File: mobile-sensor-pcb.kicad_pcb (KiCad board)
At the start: 2 copper layers, 101.6 x 53.3 mm, 27 parts, among them U1 NCP551

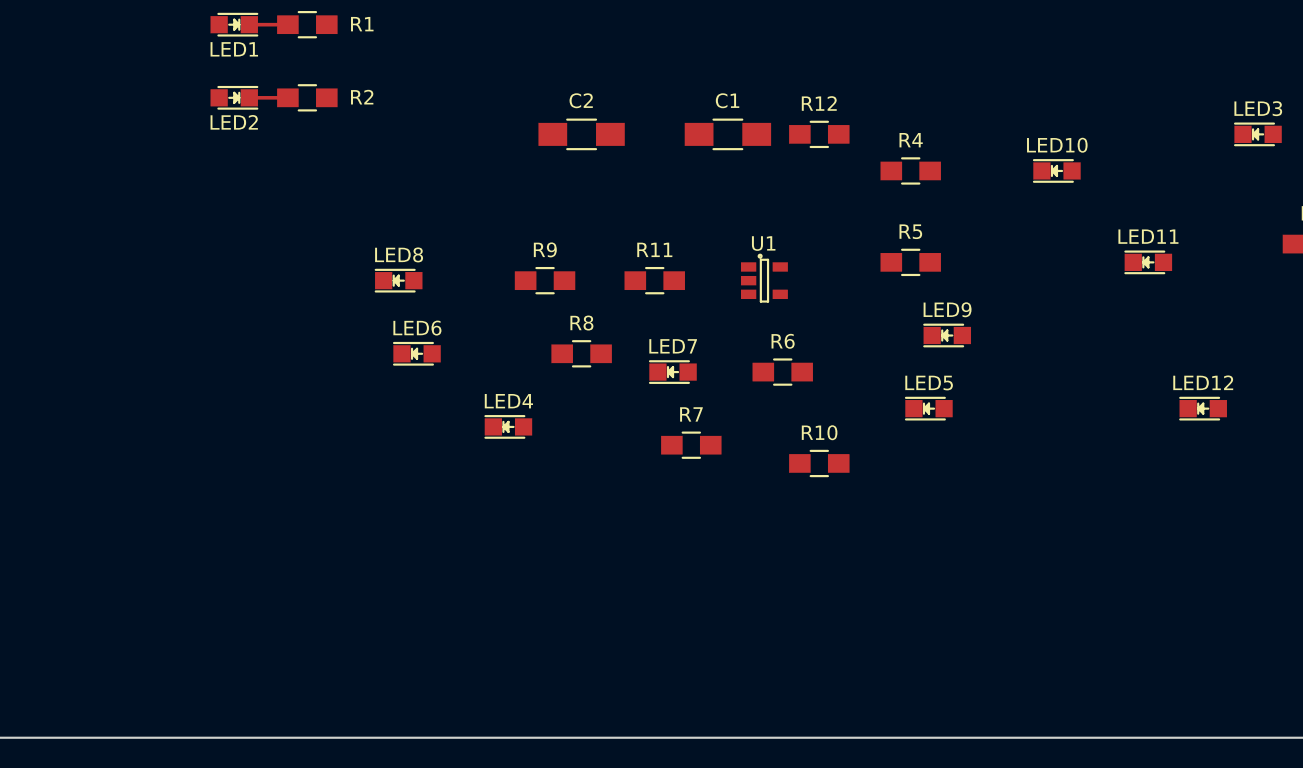
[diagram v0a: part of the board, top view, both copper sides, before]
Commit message: Add more components and footprints
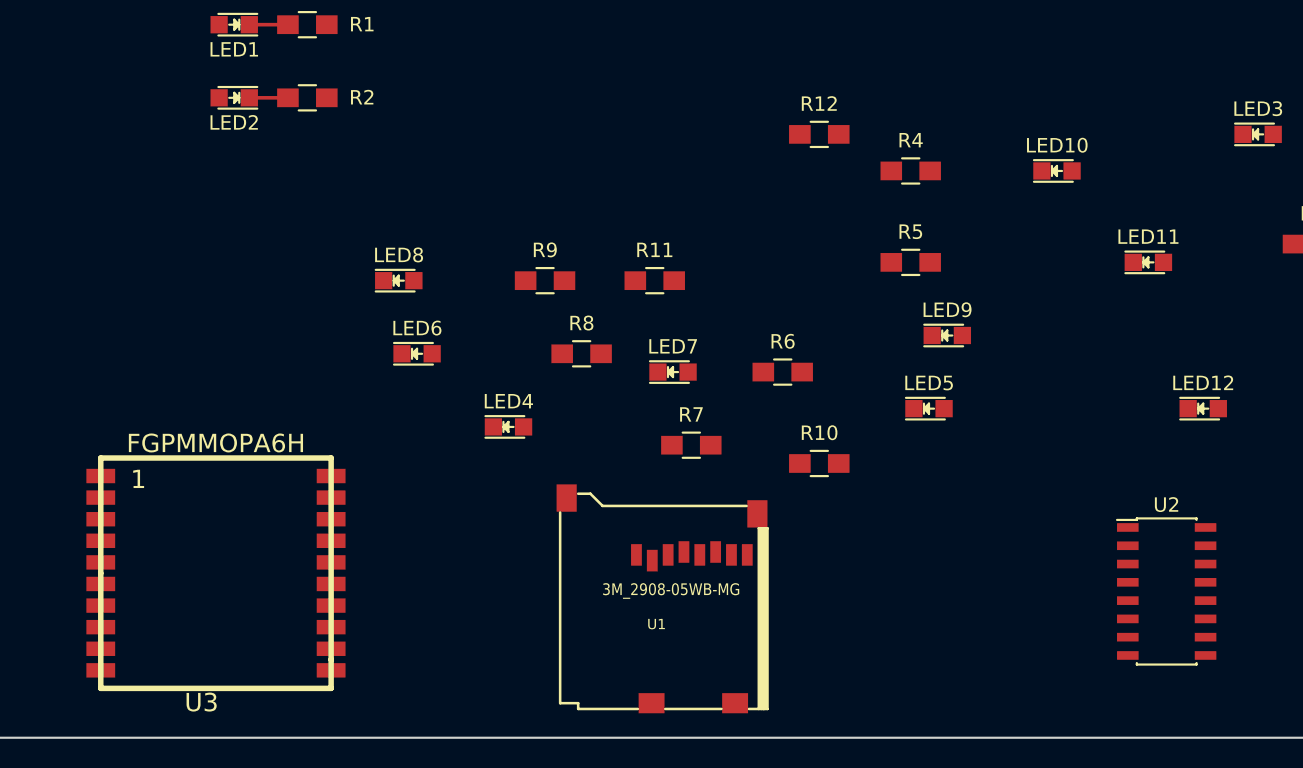
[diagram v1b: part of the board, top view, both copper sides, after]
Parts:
- removed C1: 10 uF, Capacitors_SMD:C_1206_HandSoldering
- removed C2: C_Small, Capacitors_SMD:C_1206_HandSoldering
- added U2: 74HC4050, Housings_SOIC:SOIC-16_3.9x9.9mm_Pitch1.27mm, F.Cu at (132.1, 142.2)
- added U3: FGPMMOPA6H, rascalmicro-kicad-footprints:FGPMMOPA6H, F.Cu at (66.0, 141.0)
- U1: value NCP551 -> 3M_2908-05WB-MG; footprint Housings_SOT-23_SOT-143_TSOT-6:SOT-23-5 -> rascalmicro-kicad-footprints:3M_2908-05WB-MG
- moved U1 21.0 mm to (95.2, 139.7)

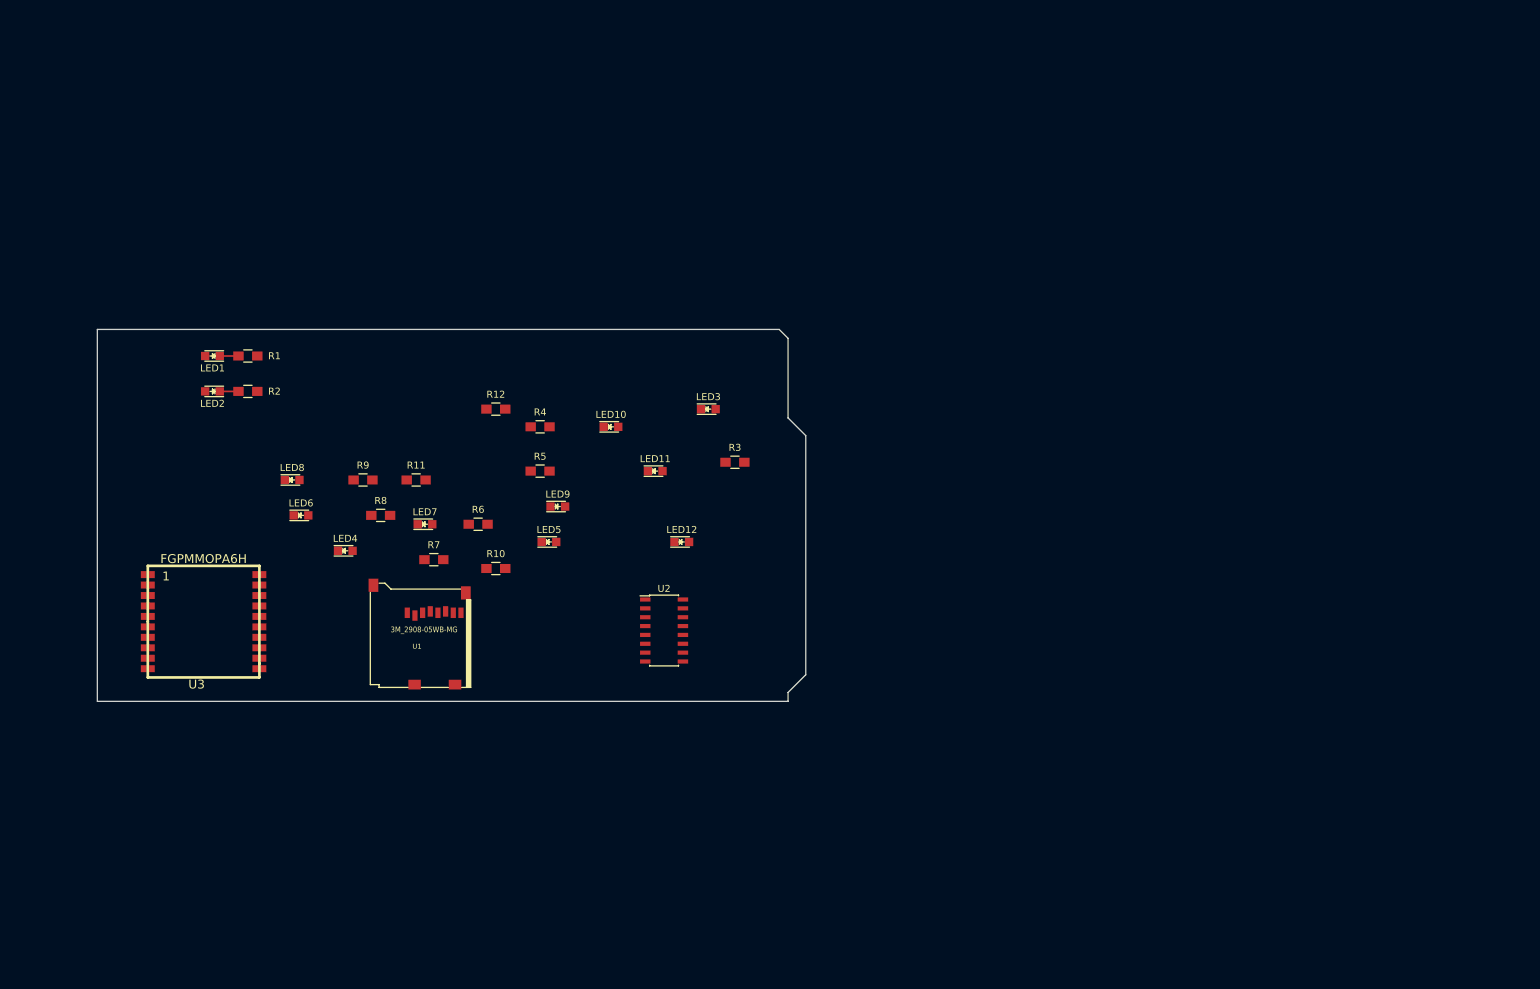
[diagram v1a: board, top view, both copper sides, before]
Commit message: More components, plus update footprint library rev
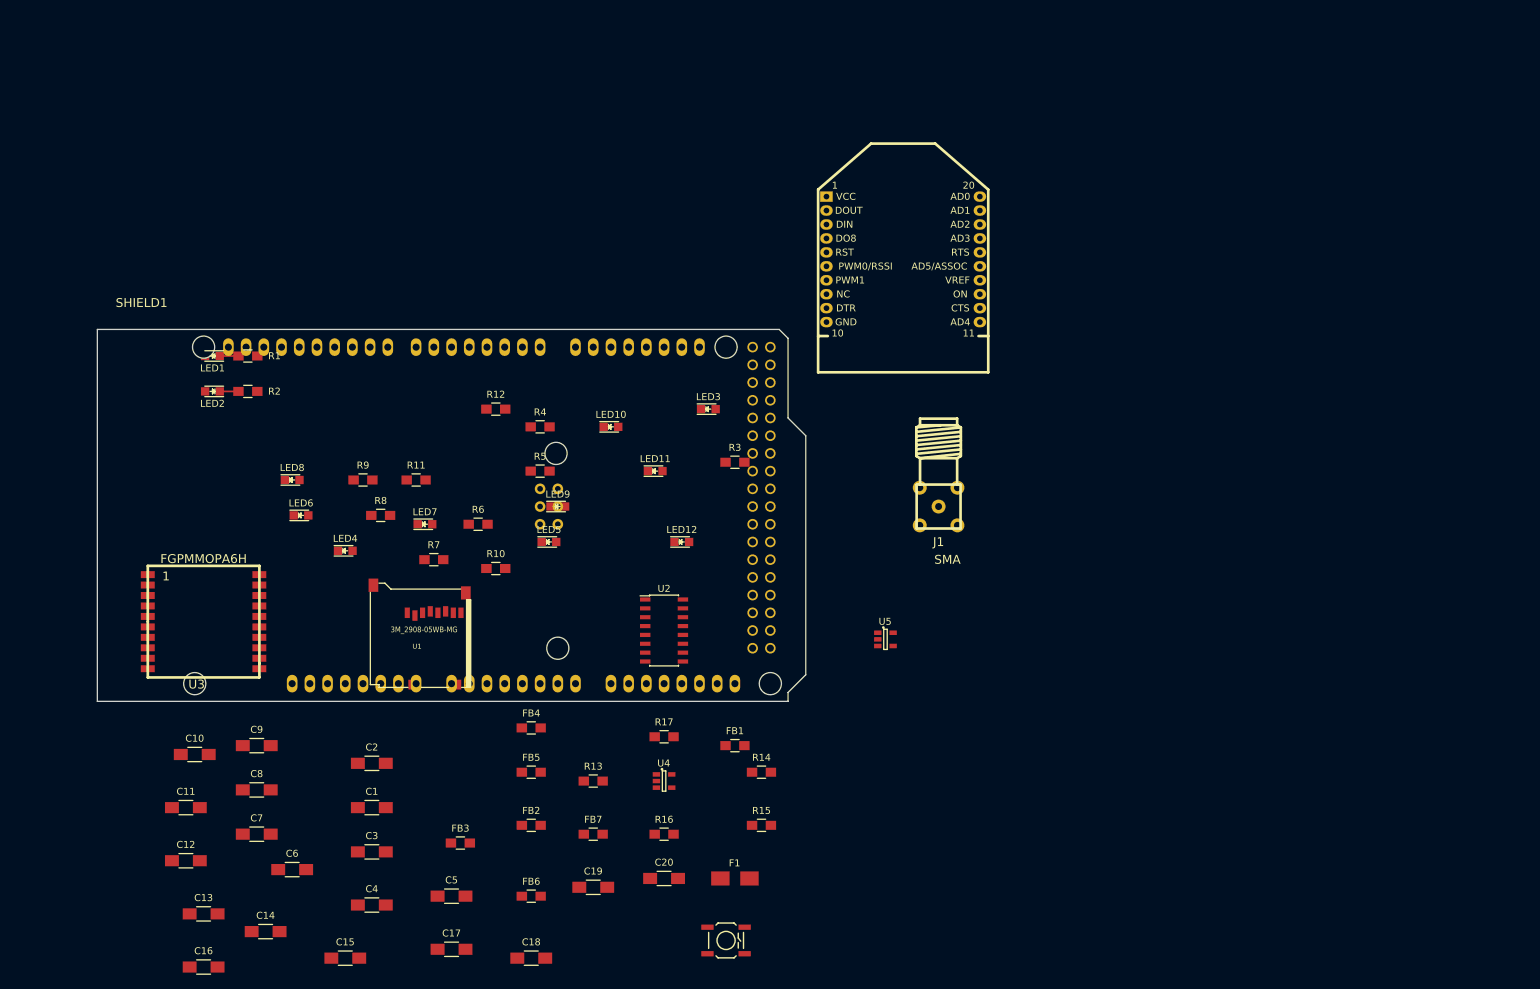
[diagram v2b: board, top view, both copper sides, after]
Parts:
- added C1: 10 uF, Capacitors_SMD:C_1206_HandSoldering, F.Cu at (90.2, 167.6)
- added C10: 10 uF, Capacitors_SMD:C_1206_HandSoldering, F.Cu at (64.8, 160.0)
- added C11: 10 uF, Capacitors_SMD:C_1206_HandSoldering, F.Cu at (63.5, 167.6)
- added C12: 10 uF, Capacitors_SMD:C_1206_HandSoldering, F.Cu at (63.5, 175.3)
- added C13: 2.2 uF, Capacitors_SMD:C_1206_HandSoldering, F.Cu at (66.0, 182.9)
- added C14: 100 nF, Capacitors_SMD:C_1206_HandSoldering, F.Cu at (74.9, 185.4)
- added C15: 100 nF, Capacitors_SMD:C_1206_HandSoldering, F.Cu at (86.4, 189.2)
- added C16: 100 nF, Capacitors_SMD:C_1206_HandSoldering, F.Cu at (66.0, 190.5)
- added C17: 10 nF, Capacitors_SMD:C_1206_HandSoldering, F.Cu at (101.6, 188.0)
- added C18: 10 nF, Capacitors_SMD:C_1206_HandSoldering, F.Cu at (113.0, 189.2)
- added C19: 10 nF, Capacitors_SMD:C_1206_HandSoldering, F.Cu at (121.9, 179.1)
- added C2: 10 uF, Capacitors_SMD:C_1206_HandSoldering, F.Cu at (90.2, 161.3)
- added C20: 100 uF, Capacitors_SMD:C_1206_HandSoldering, F.Cu at (132.1, 177.8)
- added C3: 10 uF, Capacitors_SMD:C_1206_HandSoldering, F.Cu at (90.2, 174.0)
- added C4: 10 uF, Capacitors_SMD:C_1206_HandSoldering, F.Cu at (90.2, 181.6)
- added C5: 10 uF, Capacitors_SMD:C_1206_HandSoldering, F.Cu at (101.6, 180.3)
- added C6: 10 uF, Capacitors_SMD:C_1206_HandSoldering, F.Cu at (78.7, 176.5)
- added C7: 10 uF, Capacitors_SMD:C_1206_HandSoldering, F.Cu at (73.7, 171.4)
- added C8: 10 uF, Capacitors_SMD:C_1206_HandSoldering, F.Cu at (73.7, 165.1)
- added C9: 10 uF, Capacitors_SMD:C_1206_HandSoldering, F.Cu at (73.7, 158.8)
- added F1: F_Small, Fuse_Holders_and_Fuses:Fuse_SMD1206_HandSoldering, F.Cu at (142.2, 177.8)
- added FB1: FILTER, Resistors_SMD:R_0805_HandSoldering, F.Cu at (142.2, 158.8)
- added FB2: FILTER, Resistors_SMD:R_0805_HandSoldering, F.Cu at (113.0, 170.2)
- added FB3: FILTER, Resistors_SMD:R_0805_HandSoldering, F.Cu at (102.9, 172.7)
- added FB4: FILTER, Resistors_SMD:R_0805_HandSoldering, F.Cu at (113.0, 156.2)
- added FB5: FILTER, Resistors_SMD:R_0805_HandSoldering, F.Cu at (113.0, 162.6)
- added FB6: FILTER, Resistors_SMD:R_0805_HandSoldering, F.Cu at (113.0, 180.3)
- added FB7: FILTER, Resistors_SMD:R_0805_HandSoldering, F.Cu at (121.9, 171.4)
- added J1: SMA, rascalmicro_kicad_footprints:SMA, F.Cu at (171.4, 124.5)
- added R13: 10k, Resistors_SMD:R_0805_HandSoldering, F.Cu at (121.9, 163.8)
- added R14: 10k, Resistors_SMD:R_0805_HandSoldering, F.Cu at (146.1, 162.6)
- added R15: 10k, Resistors_SMD:R_0805_HandSoldering, F.Cu at (146.1, 170.2)
- added R16: 10k, Resistors_SMD:R_0805_HandSoldering, F.Cu at (132.1, 171.4)
- added R17: 10k, Resistors_SMD:R_0805_HandSoldering, F.Cu at (132.1, 157.5)
- added SHIELD1: ARDUINO_DUE_SHIELD, freetronics_footprints:ARDUINO_DUE_SHIELD, F.Cu at (50.8, 152.4)
- added SW1: RESET, freetronics_footprints:SW_PUSHBUTTON_SMD, F.Cu at (141.0, 186.7)
- added U4: RT9193, Housings_SOT-23_SOT-143_TSOT-6:SOT-23-5, F.Cu at (132.1, 163.8)
- added U5: MIC5219, Housings_SOT-23_SOT-143_TSOT-6:SOT-23-5, F.Cu at (163.8, 143.5)
- added X1: XBEE, freetronics_footprints:XBEE_PRO, F.Cu at (166.4, 80.0)

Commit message: More components, more footprints
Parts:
- added BT1: Battery, Discret:CR1220, F.Cu at (132.1, 80.0)
- added D1: MBR120VLSFT1G, Diodes_SMD:SOD-123, F.Cu at (166.4, 154.9)
- added J2: USB_OTG, rascalmicro_kicad_footprints:USB-micro-B-female, F.Cu at (40.6, 138.4)
- added J3: JST PH, rascalmicro_kicad_footprints:s2b-ph-sm4-tb, F.Cu at (111.8, 85.1)
- added SW2: OS102011MA1QS1, rascalmicro_kicad_footprints:OS102011MA1QS1, F.Cu at (92.7, 85.1)
- added TC1: SCREW TERMINAL, freetronics_footprints:SCREWTERMINAL-3.5MM-2, F.Cu at (158.8, 163.8)
- added TC2: SCREW TERMINAL, freetronics_footprints:SCREWTERMINAL-3.5MM-2, F.Cu at (195.6, 133.3)
- added TC3: SCREW TERMINAL, freetronics_footprints:SCREWTERMINAL-3.5MM-2, F.Cu at (201.9, 143.5)
- added U10: LP2980AIM5-3.3/NOPB, Housings_SOT-23_SOT-143_TSOT-6:SOT-23-5, F.Cu at (72.4, 83.8)
- added U11: LP2980AIM5-3.3/NOPB, Housings_SOT-23_SOT-143_TSOT-6:SOT-23-5, F.Cu at (61.0, 76.2)
- added U12: LP2980AIM5-3.3/NOPB, Housings_SOT-23_SOT-143_TSOT-6:SOT-23-5, F.Cu at (81.3, 76.2)
- added U6: MCP73831T-2ACI/OT, Housings_SOT-23_SOT-143_TSOT-6:SOT-23-5, F.Cu at (185.4, 142.2)
- added U7: MAX31855KASA, Housings_SOIC:SOIC-8_3.9x4.9mm_Pitch1.27mm, F.Cu at (186.7, 119.4)
- added U8: MAX31855KASA, Housings_SOIC:SOIC-8_3.9x4.9mm_Pitch1.27mm, F.Cu at (198.1, 111.8)
- added U9: MAX31855KASA, Housings_SOIC:SOIC-8_3.9x4.9mm_Pitch1.27mm, F.Cu at (212.1, 116.8)
- F1: value F_Small -> 500 mA fuse

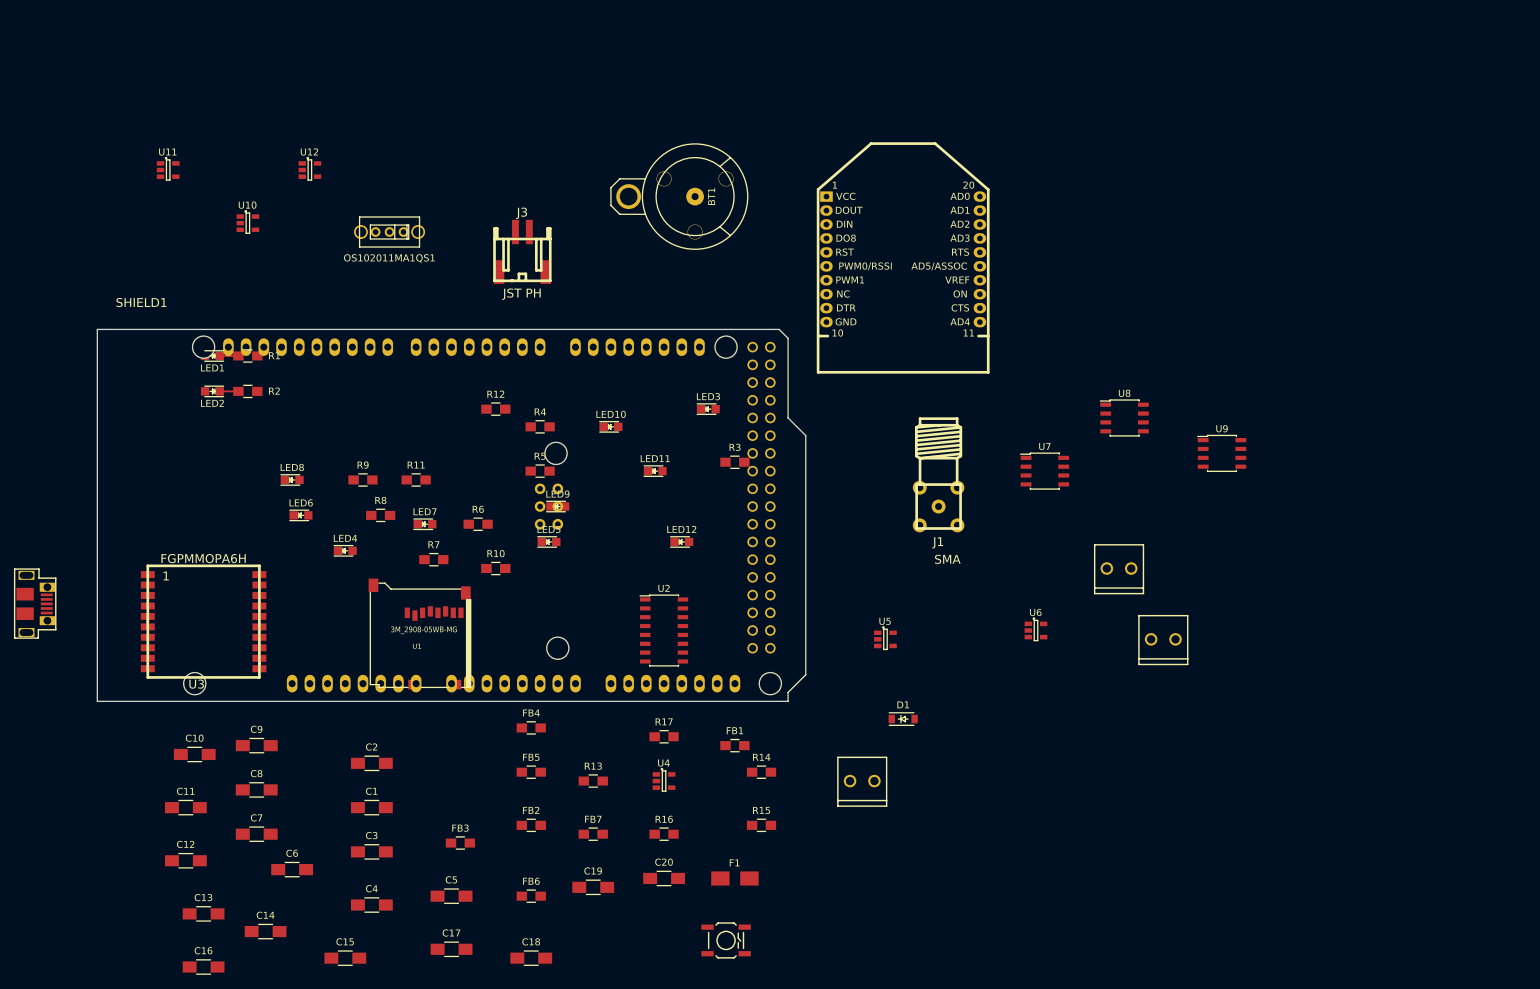
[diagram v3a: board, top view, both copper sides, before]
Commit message: First commit with all footprints added
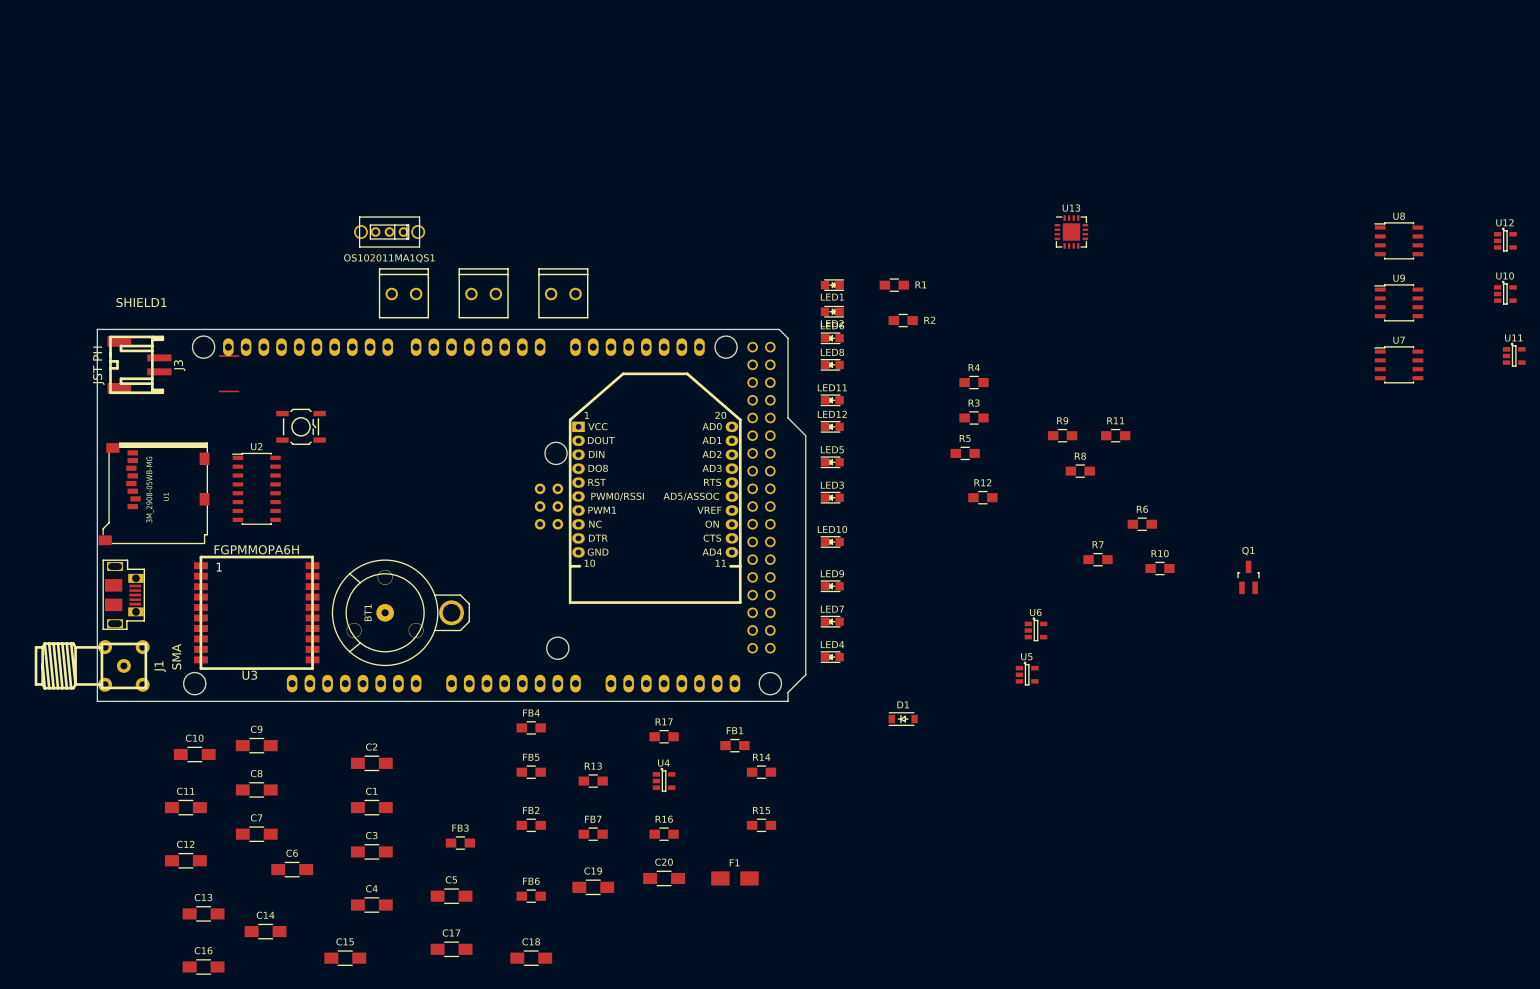
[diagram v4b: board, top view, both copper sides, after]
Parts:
- added Q1: PNP-BJT-BIASED_SOT, Housings_SOT-23_SOT-143_TSOT-6:SOT-23_Handsoldering, F.Cu at (215.9, 134.6)
- added U13: TPS61030RSA, Housings_DFN_QFN:QFN-16-1EP_4x4mm_Pitch0.65mm, F.Cu at (190.5, 85.1)
- moved U11 194.9 mm to (254.0, 102.9)
- moved U10 180.6 mm to (252.7, 94.0)
- moved U12 171.8 mm to (252.7, 86.4)
- moved J1 119.1 mm to (54.6, 147.3), turned to 90 degrees
- moved TC2 106.6 mm to (96.5, 94.0), turned to 180 degrees
- moved TC3 106.2 mm to (108.0, 94.0), turned to 180 degrees
- moved R8 100.5 mm to (191.8, 119.4)
- moved R11 100.5 mm to (196.8, 114.3)
- moved R9 100.5 mm to (189.2, 114.3)
- moved SW1 95.6 mm to (80.0, 113.0)
- moved R6 95.2 mm to (200.7, 127.0)
- moved R7 95.2 mm to (194.3, 132.1)
- moved R10 95.2 mm to (203.2, 133.3)
- moved R2 94.5 mm to (166.4, 97.8)
- moved R1 93.3 mm to (165.1, 92.7)
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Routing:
- net (no net): track 0.00 -> 5.36 mm
- net Net-(LED2-Pad1): track 2.68 -> 0.00 mm
- net Net-(LED1-Pad1): track 2.68 -> 0.00 mm
